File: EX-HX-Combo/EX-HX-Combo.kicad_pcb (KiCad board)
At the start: 2 copper layers, 150.2 x 124.5 mm, 46 parts, among them CN1 DB9 Male, J1 IDE_CONNECTOR, J2 Bus_Tandy_Plus, J3 Bus_Tandy_Plus_Through, SW1 SW_DIP_x10, U1 BIOS FLASH, U2 74HCT245, U3 1.8432 MHz, U4 DS1315, U5 AS6C4008-55PCN, U6 16550/16C550, U7 GD75232N, U8 GAL16V8, U9 GAL16V8, Y1 32.768 KHz

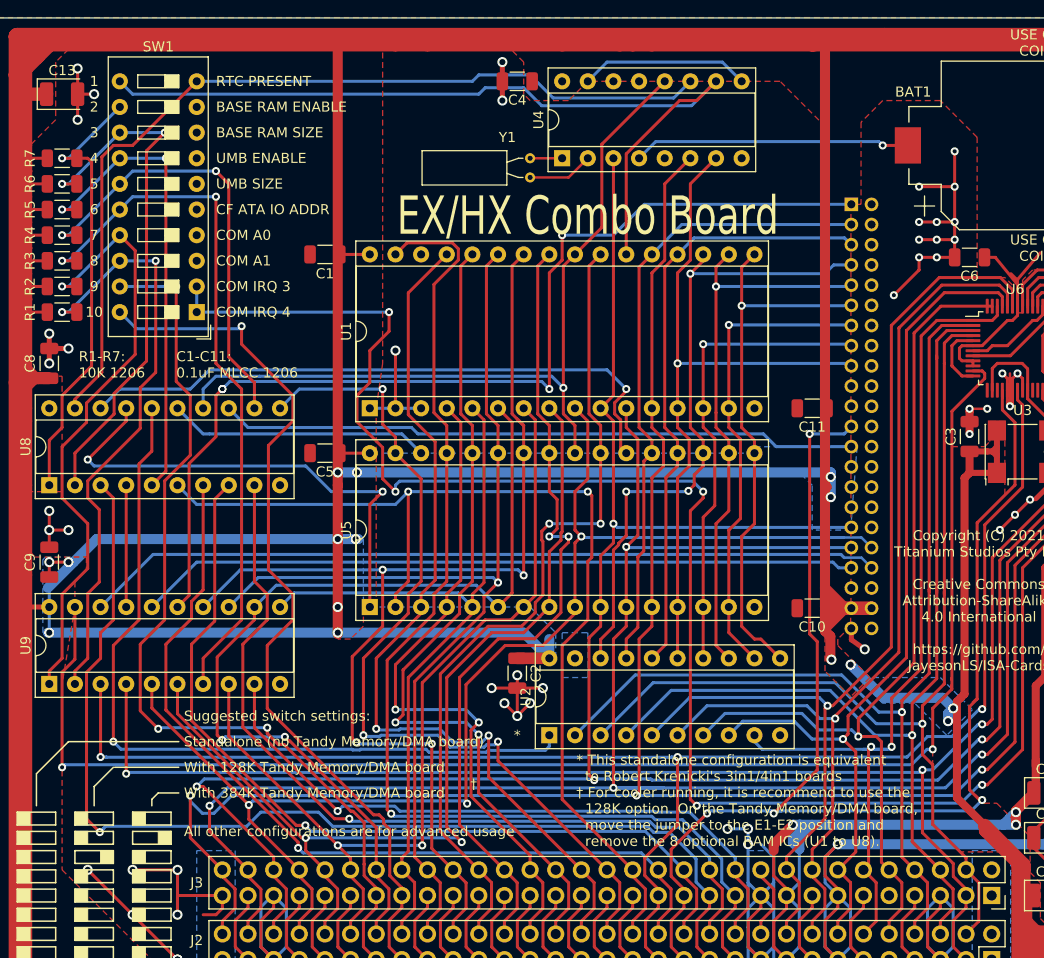
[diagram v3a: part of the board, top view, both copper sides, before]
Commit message: Lots of layout cleanup on EX-HX-Combo.
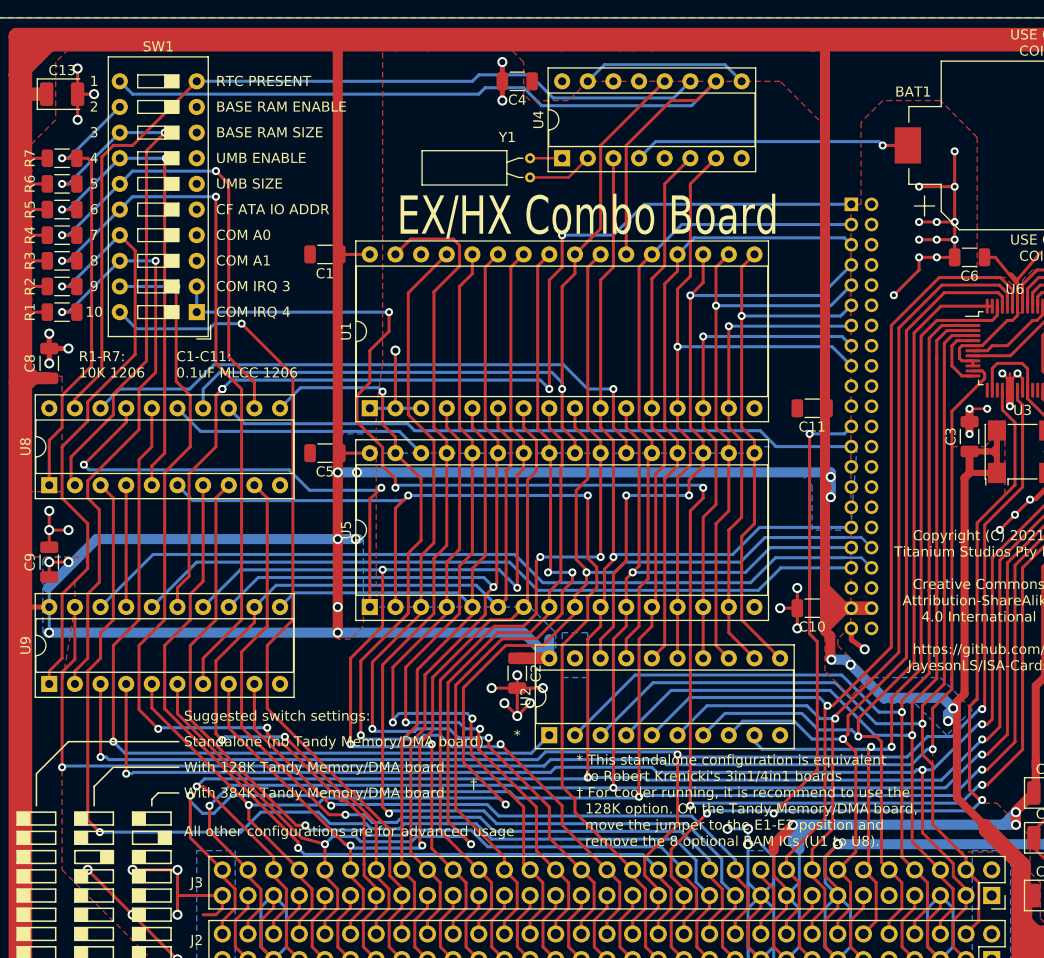
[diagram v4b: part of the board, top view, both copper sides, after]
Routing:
- net A01: track 210.4 -> 201.2 mm
- net A03: track 130.4 -> 137.5 mm
- net GND: track 250.8 -> 256.5 mm, vias 68 -> 71
- net VCC: track 1300.1 -> 1302.2 mm
- net ~CS3~_ATA: track 79.1 -> 81.1 mm
- net IRQ4: track 87.8 -> 85.8 mm
- net ~CS1~_ATA: track 71.4 -> 73.2 mm
- net ~MEMW: track 113.2 -> 114.6 mm
- net A09: track 114.0 -> 115.3 mm
- net ~CE~_RAM_DECODE: track 61.7 -> 60.5 mm
- net A12: track 66.6 -> 67.8 mm
- net D1_BUF: track 46.8 -> 48.0 mm
- net A18_MAPPED: track 50.9 -> 52.0 mm
- net D5_BUF: track 65.1 -> 66.1 mm
- net A04: track 98.4 -> 99.4 mm
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
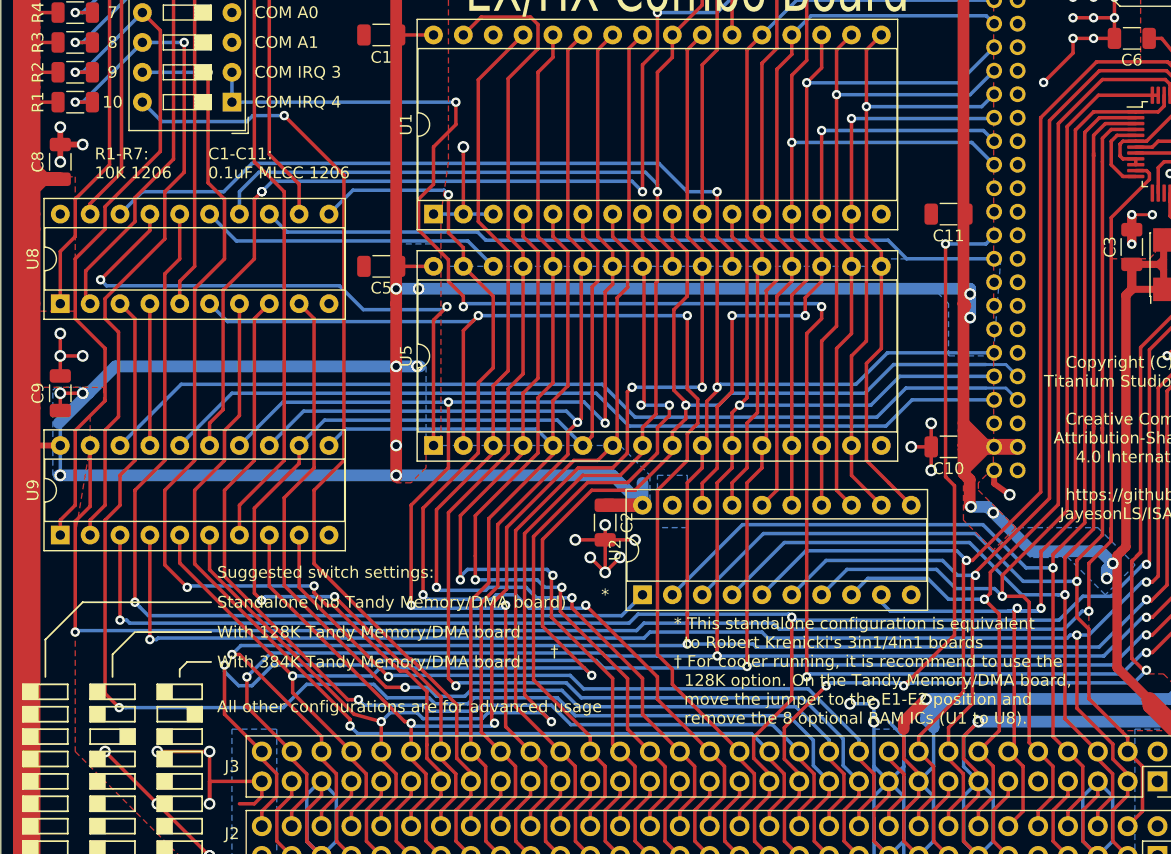
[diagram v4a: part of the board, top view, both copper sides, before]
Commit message: First pass of track layout complete on EX-HX-Combo. Still need to polish power full and vias.
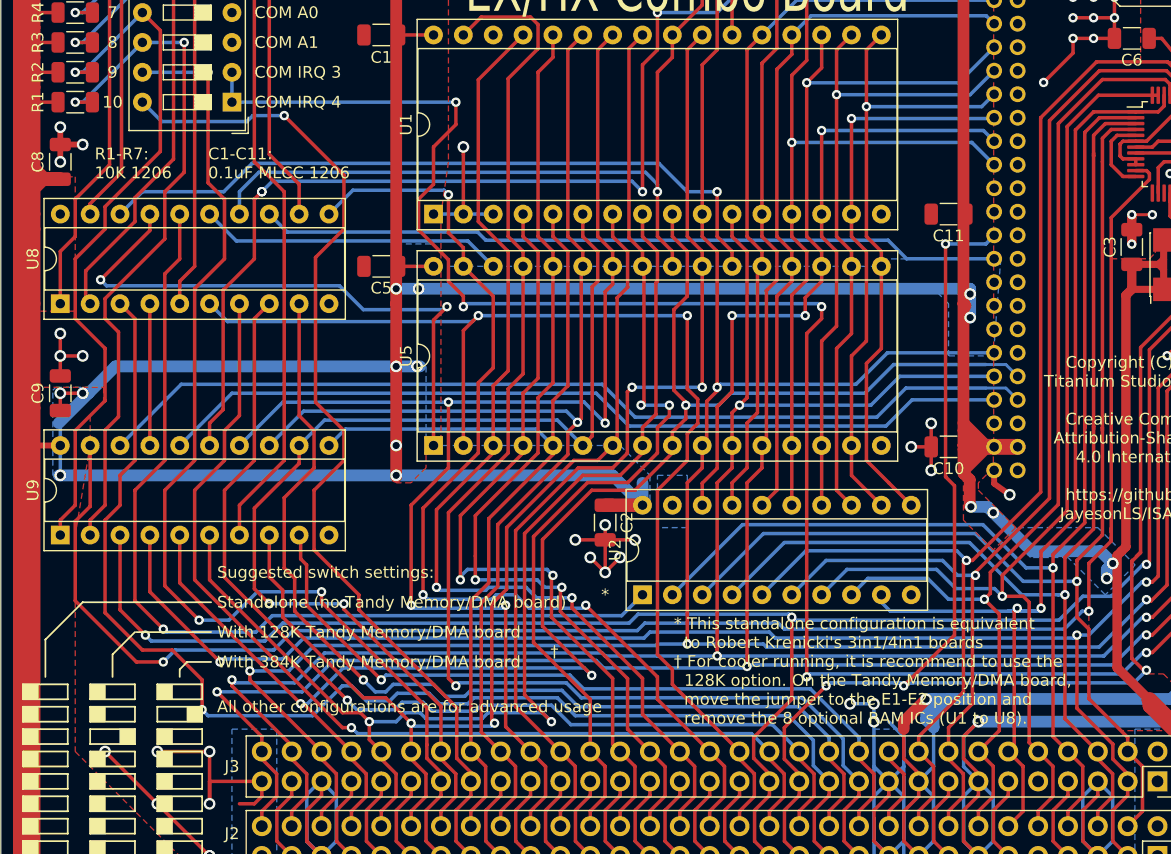
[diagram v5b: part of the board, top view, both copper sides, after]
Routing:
- net A02: track 229.9 -> 226.6 mm
- net IRQ3: track 92.9 -> 95.3 mm
- net A00: track 212.3 -> 210.1 mm
- net IRQ4: track 85.8 -> 87.7 mm
- net A01: track 201.2 -> 203.0 mm
- net ~MEMR: track 110.2 -> 108.6 mm
- net A19: track 86.1 -> 87.6 mm
- net A04: track 99.4 -> 100.5 mm
- net ~BUFF_READ: track 79.0 -> 80.1 mm
- net AEN: track 65.9 -> 66.8 mm
- net RESET: track 165.0 -> 164.2 mm
- net A05: track 88.9 -> 89.7 mm
- net ~IOR: track 153.9 -> 154.6 mm
- net A06: track 92.6 -> 92.0 mm
- net A18: track 87.7 -> 88.2 mm
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
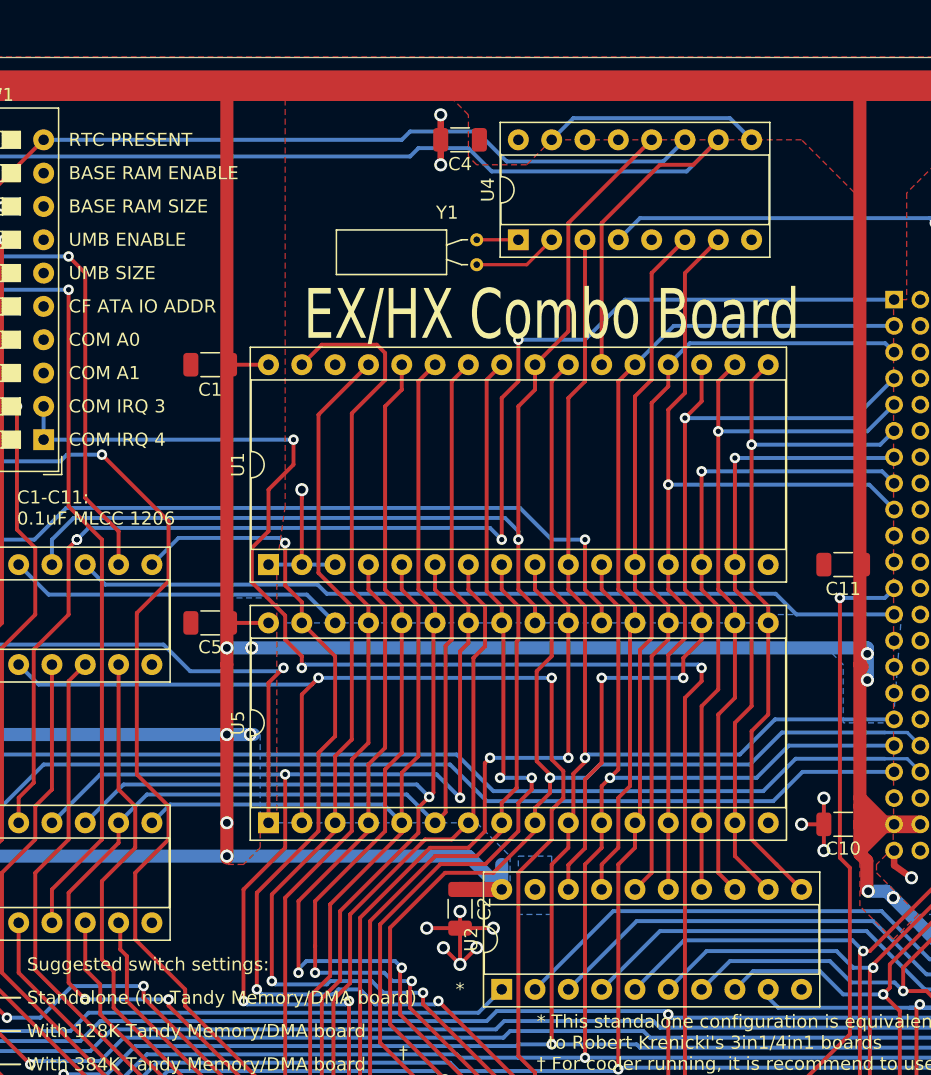
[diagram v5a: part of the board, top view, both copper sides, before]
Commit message: EX-HX-Combo power fill and via first pass completed.
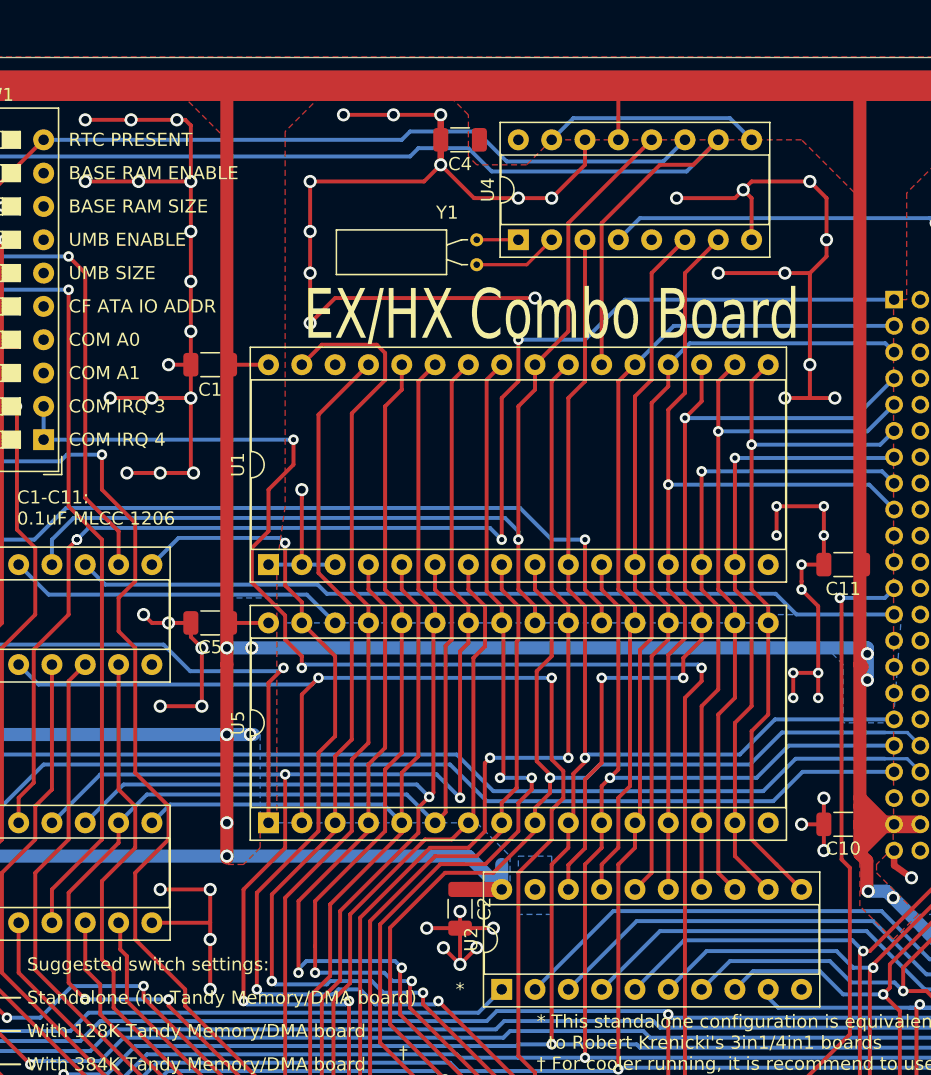
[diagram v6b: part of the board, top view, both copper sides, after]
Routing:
- net GND: track 256.5 -> 473.1 mm, vias 71 -> 124
- net VCC: track 1302.2 -> 1306.3 mm
- net IRQ4: track 87.7 -> 86.7 mm

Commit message: EX-HX-Combo: Getting close now...
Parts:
- U6: value 16550/16C550 -> 16C550
- Y1: value 32.768 KHz -> 32.768 kHz
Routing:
- net GND: track 473.1 -> 496.7 mm
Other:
- board text added: "* This standalone configuration is equivalent to Robert Krenicki's 3in1/4in1 boards † For cooler running the 128K option is recommend. On the Tandy Memory/DMA board, move the jumper to the E1-E2 position and remove the 8 optional RAM ICs (U1 to U8)."
- board text added: "100uF 16v"
- board text added: "10uF 35v"
- board text added: "32.768 kHz 6pF"
- board text added: "ATF/GAL16V8x-15 (IO Logic)"
- board text added: "ATF/GAL16V8x-15 (Mem Logic)"
- board text added: "Additional DIP switch information on back side"
- board text added: "Align center line on board and faceplate before soldering to faceplate"
- board text added: "CF Adapter"
- board text added: "Keystone 1060 or similar"
- board text added: "SERIAL"
- board text added: "SST39SF010, SST39SF020, SST39SF040 or similar"
- board text added: "Suggested DIP switch settings:"
- board text added: "Tantalum capacitors are 3528 package"
- board text removed: "* This standalone configuration is equivalent to Robert Krenicki's 3in1/4in1 boards † For cooler running, it is recommend to use the 128K option. On the Tandy Memory/DMA board, move the jumper to the E1-E2 position and remove the 8 optional RAM ICs (U1 to U8)."
- board text removed: "Additional switch information on back side"
- board text removed: "Align center line on board and faceplate before soldering faceplate"
- board text removed: "Suggested switch settings:"
